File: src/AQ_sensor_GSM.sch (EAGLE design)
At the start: 260 parts, among them J1 F-1X03-SIP-100-32, J2 53261-0871, J4 S8411-45R, Q2 MMBT2222, Q3 MMBT2222, Q4 MMBT2222, Q5 MMBT2222, Q6 MMBT2222, Q7 MMBT2222, Q8 FS8205, T1 S8050, T2 S8050, U1 CP2102N-A02-GQFN28, U2 DS1307Z, U3 TP4056, U4 TPS63802DLAR, U5 TXS0108EPWR, U6 TPS63802DLAR, X1 ESP32-S3-WROOM-1-N16R8, Y1 32.768kHz

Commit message: Routing in Progress
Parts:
- removed R40: 10K, rcl:R-EU_R0603
- added C37, C38: 0.1uF, rcl:C-EUC0603
- added L4: 784778010, Fixed Inductors:784778010
- added POWER: 10118192-0001LF, AQ_sensor_GSM:10118192-0001LF
- added R62: 100k, SparkFun-Resistors:1.20KOHM-0603-1/10W-1%
- added R63: 432k, SparkFun-Resistors:1.20KOHM-0603-1/10W-1%
- added R64: 47k, SparkFun-Resistors:1.20KOHM-0603-1/10W-1%
- added R65: 1k, SparkFun-Resistors:1.20KOHM-0603-1/10W-1%
- added R66, R67: 10K, rcl:R-EU_R0603
- added U7: TPS63802DLAR, TPS63802DLAR:TPS63802DLAR
- C21: device SparkFun-Capacitors:220PF-0402T-50V-5% -> rcl:C-EUC0603
- C26: value 22pF -> TAJB106K016RNJ; device SparkFun-Capacitors:220PF-0402T-50V-5% -> Resistor_Capacitor:TAJB106K016RNJ
- C28: value TAJB106K016RNJ -> 22pF; device Resistor_Capacitor:TAJB106K016RNJ -> rcl:C-EUC0603
- C32: value 0.1uF -> TAJB106K016RNJ; device rcl:C-EUC0603 -> Resistor_Capacitor:TAJB106K016RNJ
- renumbered 5V_IN1 to FULL, 5V_IN2 to CHRG, USB to 3.3IND
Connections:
- removed net IO15: R40.1, X1.IO15
- removed net IO5: X1.IO5
- removed net IO6: X1.IO6
- removed net IO7: X1.IO7
- removed net IO8: X1.IO8
- removed net LBV: R10.2
- removed net L_MIS0: U$1.MISO, X1.IO2
- removed net L_MOSI: U$1.MOSI, X1.IO1
- removed net L_SCK: U$1.SCK, X1.IO3
- removed net SD_CLK: MICRO_SD1.CLK, X1.IO38
- removed net SD_MISO: MICRO_SD1.CMD, X1.IO41
- removed net SD_MOSI: MICRO_SD1.DAT0, X1.IO40
- new net IO21: X1.IO21
- new net IO35: X1.IO35
- new net IO36: X1.IO36
- new net IO37: X1.IO37
- new net IO38: X1.IO38
- new net IO40: X1.IO40
- new net IO41: X1.IO41
- new net IO42: X1.IO42
- new net IO45: R66.1, X1.IO45
- new net IO46: R67.1, X1.IO46
- new net MISO: MICRO_SD1.CMD, U$1.MISO, X1.IO2
- new net MOSI: MICRO_SD1.DAT0, U$1.MOSI, X1.IO1
- new net N$149: L4.2, U7.L1
- new net N$150: L4.1, U7.L2
- new net N$151: R62.1, U7.PG
- new net N$152: R63.2, R64.1, U7.FB
- new net SPI_CLK: MICRO_SD1.CLK, U$1.SCK, X1.IO3
- net 12V-IN: now also C26.1, C28.1, C37.1, R62.2, R65.2, U7.VIN; no longer C21.1
- net 4.0V_OUT: now also C10.1, C11.1, C12.1, C13.2, C14.2, C2.1, C5.2, C6.1, C9.1, D2.K, EC200_GSM.VBAT_BB, EC200_GSM.VBAT_RF, MODE.A, MRI.A, NST.A, PST.A, R502.2
- net BOOST_EN: now also R65.1, U7.EN
- net DHT_LED: no longer X1.IO37
- net DHT_OUT: now also X1.IO7; no longer X1.IO36
- net GND: now also C37.2, C38.2, POWER.GND, POWER.ID, POWER.SHIELD, R64.2, R66.2, R67.2, U7.AGND, U7.GND, U7.MODE; no longer R40.2
- net GSM_RST_O: now also X1.IO15; no longer X1.IO42
- net L_NSS: now also X1.IO8; no longer X1.IO46
- net N$138: no longer C28.1, C32.1
- net PMS_LED: no longer X1.IO35
- net PMS_RX: now also X1.IO5; no longer X1.IO21
- net PMS_TX: now also X1.IO6; no longer X1.IO45
- net VUSB: now also C21.1, C32.1, C38.1, POWER.VUSB, R63.1, U7.VOUT; no longer C26.1
- net V_LIPO: now also R10.2; no longer C10.1, C11.1, C12.1, C13.2, C14.2, C2.1, C5.2, C6.1, C9.1, D2.K, EC200_GSM.VBAT_BB, EC200_GSM.VBAT_RF, MODE.A, MRI.A, NST.A, PST.A, R502.2
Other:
- note added: "5V In Buck CIRCUIT"
- moved on the sheet: C21, C26, C27, C28, C32, GRST, GSM_RST, MODE, MRI, NST, PST, Q4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

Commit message: 90% routed
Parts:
- removed DHT: GREEN, led:LEDCHIP-LED0603
- removed PMS: ORANGE, led:LEDCHIP-LED0603
- removed R11, R49: 200, rcl:R-EU_R0603
- removed R16, R4: 470R, rcl:R-EU_R0603
- removed RXT, TXT: (no value), led:LEDCHIP-LED0603
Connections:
- removed net DHT_LED: R16.2
- removed net N$115: U$69.P$1, U1.GPIO.3/WAKEUP
- removed net N$116: U$68.P$1, U1.GPIO.4
- removed net N$117: U$67.P$1, U1.GPIO.5
- removed net N$118: U$66.P$1, U1.GPIO.6
- removed net PMS_LED: R4.2
- net +3V3: no longer R11.2, R49.2
- net GND: no longer DHT.C, PMS.C, RST2.SHIELD
- net N$114: now also U$71.P$1, U1.GPIO.6; no longer U$70.P$1, U1.GPIO.2/RS485
- net N$27: now also U$70.P$1, U1.GPIO.1/RXT; no longer DHT.A, R16.1
- net N$4: now also U$72.P$1, U1.GPIO.0/TXT; no longer PMS.A, R4.1
- net N$54: now also U$69.P$1, U1.GPIO.2/RS485; no longer R11.1, TXT.C
- net N$55: now also U$68.P$1, U1.GPIO.3/WAKEUP; no longer R49.1, RXT.C
- net N$56: now also U$67.P$1, U1.GPIO.4; no longer TXT.A, U1.GPIO.0/TXT
- net N$57: now also U$66.P$1, U1.GPIO.5; no longer RXT.A, U1.GPIO.1/RXT
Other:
- note removed: "IO6 TO IO11 ARE USED BY SPIFFS AND CANT BE USED"

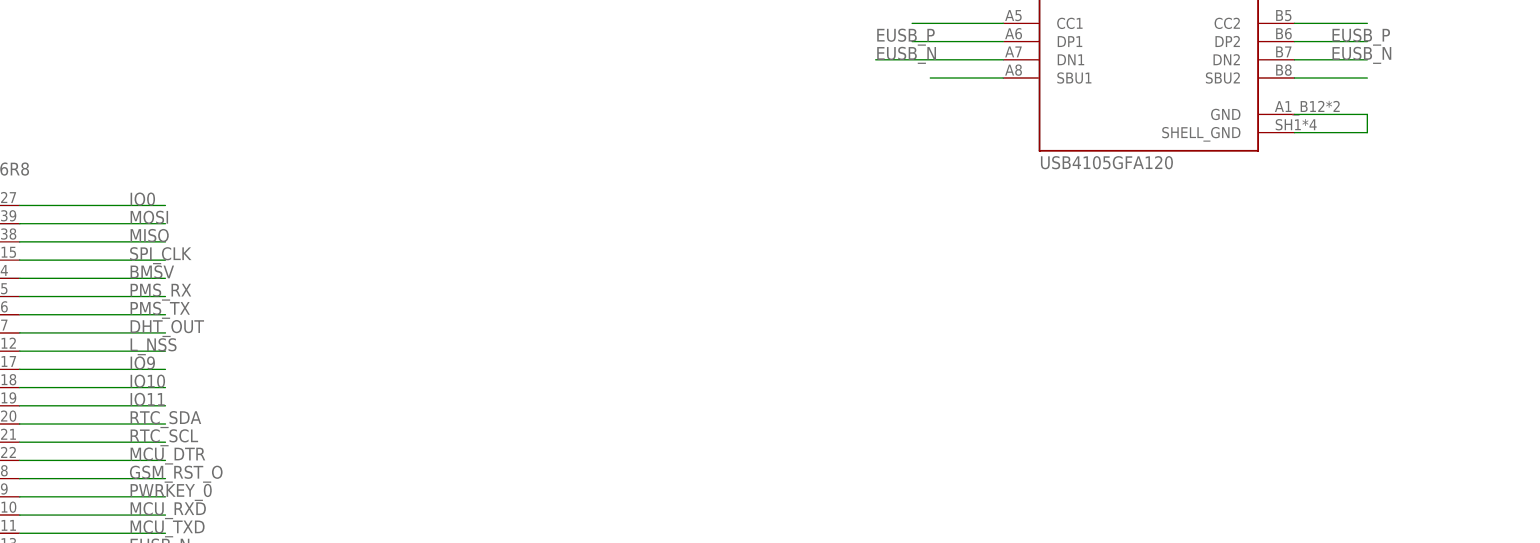
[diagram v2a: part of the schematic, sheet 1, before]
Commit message: 100% routed Minus Board Outline
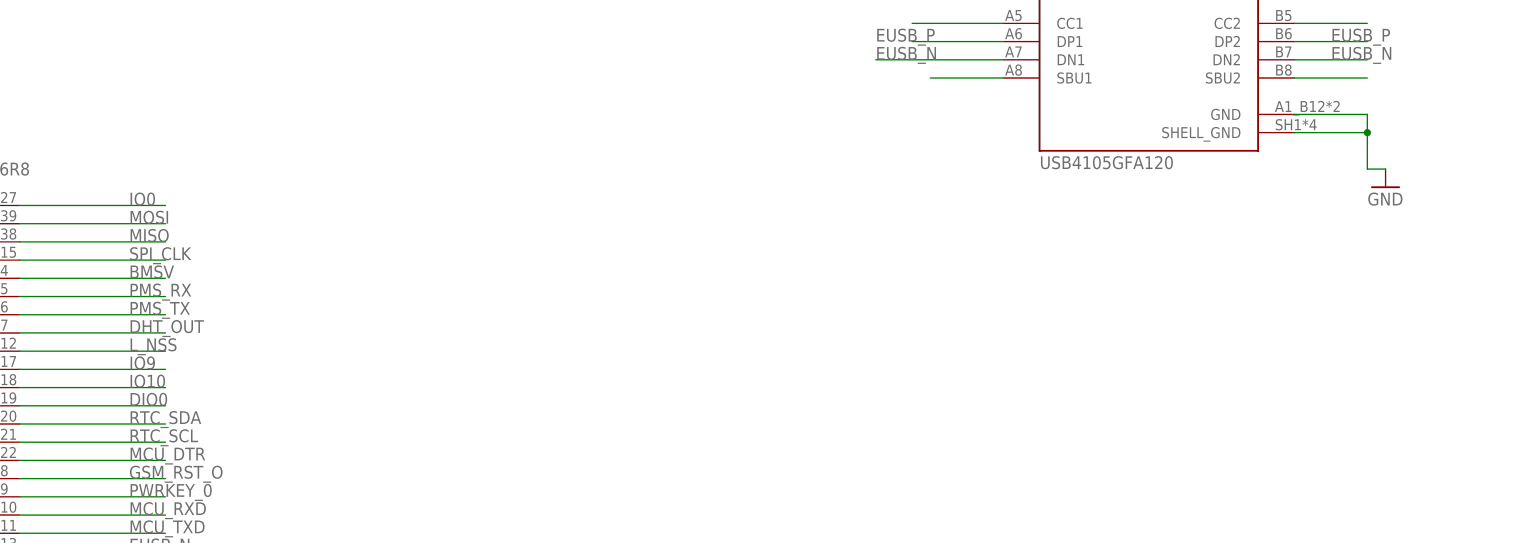
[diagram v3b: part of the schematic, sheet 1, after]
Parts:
- removed U$75: NC_MARKER, NC_MARKER:NC_MARKER
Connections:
- removed net IO11: X1.IO11
- removed net N$128: U$1.DIO0, U$75.P$1
- removed net N$140: JTAG.GND, JTAG.SHELL_GND
- new net DIO0: U$1.DIO0, X1.IO11
- net GND: now also JTAG.GND, JTAG.SHELL_GND
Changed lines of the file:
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@@
 <part name="U$73" library="NC_MARKER" deviceset="NC_MARKER" device=""/>
 <part name="U$74" library="NC_MARKER" deviceset="NC_MARKER" device=""/>
-<part name="U$75" library="NC_MARKER" deviceset="NC_MARKER" device=""/>
 <part name="U$76" library="NC_MARKER" deviceset="NC_MARKER" device=""/>
 <part name="U$77" library="NC_MARKER" deviceset="NC_MARKER" device=""/>
@@
 <part name="GND97" library="supply1" library_urn="urn:adsk.eagle:library:371" deviceset="GND" device=""/>
 <part name="R67" library="rcl" library_urn="urn:adsk.eagle:library:334" deviceset="R-EU_" device="R0603" package3d_urn="urn:adsk.eagle:package:23555/3" value="10K"/>
+<part name="GND8" library="supply1" library_urn="urn:adsk.eagle:library:371" deviceset="GND" device=""/>
 </parts>
 <sheets>
@@
 <attribute name="VALUE" x="37.338" y="227.33" size="1.778" layer="96" rot="R270"/>
 </instance>
+<instance part="GND8" gate="1" x="281.94" y="165.1" smashed="yes">
+<attribute name="VALUE" x="279.4" y="162.56" size="1.778" layer="96"/>
+</instance>
 </instances>
 <busses>
@@
 <pinref part="R67" gate="G$1" pin="2"/>
 </segment>
+<segment>
+<pinref part="JTAG" gate="G$1" pin="SHELL_GND"/>
+<wire x1="269.24" y1="172.72" x2="279.4" y2="172.72" width="0.1524" layer="91"/>
+<wire x1="279.4" y1="172.72" x2="279.4" y2="175.26" width="0.1524" layer="91"/>
+<pinref part="JTAG" gate="G$1" pin="GND"/>
+<wire x1="279.4" y1="175.26" x2="269.24" y2="175.26" width="0.1524" layer="91"/>
+<pinref part="GND8" gate="1" pin="GND"/>
+<wire x1="281.94" y1="167.64" x2="279.4" y2="167.64" width="0.1524" layer="91"/>
+<wire x1="279.4" y1="167.64" x2="279.4" y2="172.72" width="0.1524" layer="91"/>
+<junction x="279.4" y="172.72"/>
+</segment>
 </net>
 <net name="+3V3" class="1">
@@
 </segment>
 </net>
-<net name="IO11" class="0">
+<net name="DIO0" class="0">
 <segment>
 <pinref part="X1" gate="G$1" pin="IO11"/>
@@
 </segment>
 </net>
-<net name="N$140" class="0">
-<segment>
-<pinref part="JTAG" gate="G$1" pin="SHELL_GND"/>
-<wire x1="269.24" y1="172.72" x2="279.4" y2="172.72" width="0.1524" layer="91"/>
-<wire x1="279.4" y1="172.72" x2="279.4" y2="175.26" width="0.1524" layer="91"/>
-<pinref part="JTAG" gate="G$1" pin="GND"/>
-<wire x1="279.4" y1="175.26" x2="269.24" y2="175.26" width="0.1524" layer="91"/>
-</segment>
-</net>
 <net name="N$141" class="0">
 <segment>
@@
 <attribute name="VALUE" x="16.518" y="12.478" size="1.778" layer="96" rot="R270"/>
 </instance>
-<instance part="U$75" gate="G$1" x="27.94" y="10.16" smashed="yes"/>
 <instance part="U$76" gate="G$1" x="27.94" y="7.62" smashed="yes"/>
 <instance part="U$77" gate="G$1" x="27.94" y="5.08" smashed="yes"/>
@@
 </segment>
 </net>
-<net name="N$128" class="0">
+<net name="DIO0" class="0">
 <segment>
-<pinref part="U$75" gate="G$1" pin="P$1"/>
 <pinref part="U$1" gate="G$1" pin="DIO0"/>
 <wire x1="33.02" y1="10.16" x2="35.56" y2="10.16" width="0.1524" layer="91"/>
+<label x="27.94" y="10.16" size="1.778" layer="95"/>
 </segment>
 </net>

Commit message: Resolved multiple shared output pins
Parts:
- added R11, R4: 0.4R, Resistor_Capacitor:CRCW08050000Z0EA
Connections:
- new net N$115: R4.2, U7.VOUT
- new net N$116: 5V_REG_1.OUTPUT, R11.2
- net VUSB: now also R11.1, R4.1; no longer 5V_REG_1.OUTPUT, U7.VOUT
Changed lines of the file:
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@@
 <setting verticaltext="up"/>
 </settings>
-<grid distance="0.1" unitdist="inch" unit="inch" style="lines" multiple="1" display="no" altdistance="0.01" altunitdist="inch" altunit="inch"/>
+<grid distance="0.1" unitdist="inch" unit="inch" style="lines" multiple="1" display="no" altdistance="0.01" altunitdist="inch" altunit="mm"/>
 <layers>
 <layer number="1" name="Top" color="4" fill="1" visible="no" active="no"/>
@@
 <part name="R67" library="rcl" library_urn="urn:adsk.eagle:library:334" deviceset="R-EU_" device="R0603" package3d_urn="urn:adsk.eagle:package:23555/3" value="10K"/>
 <part name="GND8" library="supply1" library_urn="urn:adsk.eagle:library:371" deviceset="GND" device=""/>
+<part name="R4" library="Resistor_Capacitor" library_urn="urn:adsk.eagle:library:15122775" deviceset="CRCW08050000Z0EA" device="" package3d_urn="urn:adsk.eagle:package:10872899/3" value="0.4R"/>
+<part name="R11" library="Resistor_Capacitor" library_urn="urn:adsk.eagle:library:15122775" deviceset="CRCW08050000Z0EA" device="" package3d_urn="urn:adsk.eagle:package:10872899/3" value="0.4R"/>
 </parts>
 <sheets>
@@
 <attribute name="VALUE" x="48.26848125" y="393.7" size="1.78096875" layer="96" rot="R90"/>
 </instance>
-<instance part="GND13" gate="1" x="22.86" y="324.358" smashed="yes">
-<attribute name="VALUE" x="20.32" y="321.818" size="1.778" layer="96"/>
+<instance part="GND13" gate="1" x="35.56" y="324.358" smashed="yes">
+<attribute name="VALUE" x="33.02" y="321.818" size="1.778" layer="96"/>
 </instance>
 <instance part="U3" gate="G$1" x="-142.24" y="347.98" smashed="yes">
@@
 <attribute name="VALUE" x="104.14" y="260.604" size="1.778" layer="96" font="vector" rot="R180" align="top-center"/>
 </instance>
+<instance part="R4" gate="G$1" x="149.86" y="264.16" smashed="yes" rot="R180">
+<attribute name="NAME" x="153.67" y="262.6614" size="1.778" layer="95" rot="R180"/>
+<attribute name="VALUE" x="153.67" y="267.462" size="1.778" layer="96" rot="R180"/>
+</instance>
+<instance part="R11" gate="G$1" x="-236.22" y="373.38" smashed="yes" rot="R180">
+<attribute name="NAME" x="-232.41" y="371.8814" size="1.778" layer="95" rot="R180"/>
+<attribute name="VALUE" x="-232.41" y="376.682" size="1.778" layer="96" rot="R180"/>
+</instance>
 </instances>
 <busses>
@@
 </segment>
 <segment>
-<pinref part="GND13" gate="1" pin="GND"/>
-<wire x1="22.86" y1="326.898" x2="22.86" y2="329.946" width="0.1524" layer="91"/>
-<pinref part="C12" gate="G$1" pin="2"/>
-<pinref part="C9" gate="G$1" pin="2"/>
-<wire x1="24.384" y1="329.946" x2="35.56" y2="329.946" width="0.1524" layer="91"/>
-<junction x="24.384" y="329.946"/>
-<wire x1="12.7" y1="329.946" x2="24.384" y2="329.946" width="0.1524" layer="91"/>
-<pinref part="C13" gate="G$1" pin="1"/>
-<wire x1="12.7" y1="330.2" x2="12.7" y2="329.946" width="0.1524" layer="91"/>
-<junction x="12.7" y="330.2"/>
-<wire x1="2.54" y1="330.2" x2="12.7" y2="330.2" width="0.1524" layer="91"/>
-<pinref part="C2" gate="G$1" pin="2"/>
-<wire x1="22.86" y1="330.2" x2="22.86" y2="329.946" width="0.1524" layer="91"/>
-<wire x1="22.86" y1="329.946" x2="24.384" y2="329.946" width="0.1524" layer="91"/>
-</segment>
-<segment>
 <pinref part="GND1" gate="1" pin="GND"/>
 <wire x1="-238.76" y1="362.458" x2="-238.76" y2="365.76" width="0.1524" layer="91"/>
@@
 <wire x1="162.56" y1="236.22" x2="162.56" y2="238.76" width="0.1524" layer="91"/>
 </segment>
+<segment>
+<pinref part="C2" gate="G$1" pin="2"/>
+<pinref part="C13" gate="G$1" pin="1"/>
+<wire x1="2.54" y1="330.2" x2="12.7" y2="330.2" width="0.1524" layer="91"/>
+<pinref part="C9" gate="G$1" pin="2"/>
+<wire x1="12.7" y1="330.2" x2="12.7" y2="329.946" width="0.1524" layer="91"/>
+<wire x1="12.7" y1="329.946" x2="24.384" y2="329.946" width="0.1524" layer="91"/>
+<junction x="12.7" y="330.2"/>
+<pinref part="C12" gate="G$1" pin="2"/>
+<wire x1="24.384" y1="329.946" x2="35.56" y2="329.946" width="0.1524" layer="91"/>
+<junction x="24.384" y="329.946"/>
+<pinref part="GND13" gate="1" pin="GND"/>
+<wire x1="35.56" y1="326.898" x2="35.56" y2="329.946" width="0.1524" layer="91"/>
+<junction x="35.56" y="329.946"/>
+</segment>
 </net>
 <net name="V_LIPO" class="3">
@@
 </segment>
 <segment>
-<pinref part="5V_REG_1" gate="G$1" pin="OUTPUT"/>
-<wire x1="-246.38" y1="373.38" x2="-238.76" y2="373.38" width="0.1524" layer="91"/>
-<label x="-243.84" y="373.38" size="1.778" layer="95"/>
-</segment>
-<segment>
 <pinref part="5V_JST" gate="G$1" pin="1"/>
 <wire x1="-276.86" y1="304.8" x2="-292.1" y2="304.8" width="0.1524" layer="91"/>
@@
 </segment>
 <segment>
-<pinref part="U7" gate="G$1" pin="VOUT"/>
 <pinref part="C38" gate="G$1" pin="1"/>
-<wire x1="142.24" y1="264.16" x2="162.56" y2="264.16" width="0.1524" layer="91"/>
 <wire x1="162.56" y1="264.16" x2="172.72" y2="264.16" width="0.1524" layer="91"/>
 <wire x1="172.72" y1="264.16" x2="172.72" y2="259.08" width="0.1524" layer="91"/>
@@
 <pinref part="R63" gate="G$1" pin="1"/>
 <wire x1="162.56" y1="261.62" x2="162.56" y2="264.16" width="0.1524" layer="91"/>
-<junction x="162.56" y="264.16"/>
 <wire x1="180.34" y1="264.16" x2="198.12" y2="264.16" width="0.1524" layer="91"/>
 <junction x="180.34" y="264.16"/>
 <label x="187.96" y="264.16" size="1.778" layer="95"/>
+<pinref part="R4" gate="G$1" pin="1"/>
+<wire x1="154.94" y1="264.16" x2="162.56" y2="264.16" width="0.1524" layer="91"/>
+<junction x="162.56" y="264.16"/>
+</segment>
+<segment>
+<pinref part="R11" gate="G$1" pin="1"/>
+<wire x1="-231.14" y1="373.38" x2="-223.52" y2="373.38" width="0.1524" layer="91"/>
+<label x="-228.6" y="373.38" size="1.778" layer="95"/>
 </segment>
 </net>
@@
 <pinref part="C13" gate="G$1" pin="2"/>
 <wire x1="2.54" y1="337.82" x2="12.7" y2="337.82" width="0.1524" layer="91"/>
-<wire x1="12.7" y1="337.82" x2="12.7" y2="345.44" width="0.1524" layer="91"/>
+<wire x1="12.7" y1="337.82" x2="12.7" y2="340.36" width="0.1524" layer="91"/>
+<wire x1="12.7" y1="340.36" x2="12.7" y2="345.44" width="0.1524" layer="91"/>
 <wire x1="12.7" y1="345.44" x2="25.4" y2="345.44" width="0.1524" layer="91"/>
 <junction x="12.7" y="337.82"/>
@@
 <pinref part="C2" gate="G$1" pin="1"/>
 <pinref part="C12" gate="G$1" pin="1"/>
-<wire x1="35.56" y1="340.36" x2="35.56" y2="337.566" width="0.1524" layer="91"/>
+<wire x1="35.56" y1="337.566" x2="35.56" y2="340.36" width="0.1524" layer="91"/>
+<wire x1="35.56" y1="340.36" x2="12.7" y2="340.36" width="0.1524" layer="91"/>
+<junction x="12.7" y="340.36"/>
 <pinref part="C9" gate="G$1" pin="1"/>
-<wire x1="35.56" y1="340.36" x2="24.384" y2="340.36" width="0.1524" layer="91"/>
-<wire x1="24.384" y1="340.36" x2="24.384" y2="337.566" width="0.1524" layer="91"/>
-<wire x1="24.384" y1="340.36" x2="12.7" y2="340.36" width="0.1524" layer="91"/>
-<wire x1="12.7" y1="340.36" x2="12.7" y2="337.82" width="0.1524" layer="91"/>
+<wire x1="24.384" y1="337.566" x2="35.56" y2="337.566" width="0.1524" layer="91"/>
+<junction x="35.56" y="337.566"/>
 </segment>
 </net>
@@
 </segment>
 </net>
+<net name="N$115" class="0">
+<segment>
+<pinref part="U7" gate="G$1" pin="VOUT"/>
+<pinref part="R4" gate="G$1" pin="2"/>
+<wire x1="144.78" y1="264.16" x2="142.24" y2="264.16" width="0.1524" layer="91"/>
+</segment>
+</net>
+<net name="N$116" class="0">
+<segment>
+<pinref part="5V_REG_1" gate="G$1" pin="OUTPUT"/>
+<pinref part="R11" gate="G$1" pin="2"/>
+<wire x1="-241.3" y1="373.38" x2="-246.38" y2="373.38" width="0.1524" layer="91"/>
+</segment>
+</net>

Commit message: Route PCB 100%
Add 5V buck boost converter for charging Side

Add boost converter for 4.0V voltage rail

Add 5V Boost converter for the 5V rail

Add 3.3V LDO to power MCU
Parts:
- added JUMP4V, JUMP5V, JUMPVL, R16, R40: 0.4R, Resistor_Capacitor:CRCW08050000Z0EA
- added U$100, U$101, U$102, U$103, U$104, U$105, U$106, U$75, U$85, U$86, U$87, U$88, U$89, U$90, U$91, U$92, U$93, U$94, U$95, U$96, U$97, U$98, U$99: NC_MARKER, NC_MARKER:NC_MARKER
- added U8: AMS1117-3.3, AMS1117-3.3:AMS1117-3.3
- LORA: value (none) -> NA
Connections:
- removed net G_GPIO1: EC200_GSM.GPIO1
- new net N$117: JUMPVL.1, R40.1, U8.VIN
- new net N$118: R16.2, U8.VOUT
- new net N$128: EC200_GSM.GPIO1, U$75.P$1
- new net N$140: J2.1, U$103.P$1
- new net N$153: J2.2, U$102.P$1
- new net N$154: J2.3, U$104.P$1
- new net N$155: J2.6, U$105.P$1
- net +3V3: now also R16.1
- net 4.0V_OUT: now also JUMP4V.1
- net 5V_OUT: now also JUMP5V.1, R40.2
- net GND: now also U8.GND/ADJ
- net IO10: now also U$86.P$1
- net IO21: now also U$87.P$1
- net IO35: now also U$88.P$1
- net IO36: now also U$89.P$1
- net IO37: now also U$90.P$1
- net IO38: now also U$91.P$1
- net IO40: now also U$92.P$1
- net IO41: now also U$93.P$1
- net IO42: now also U$94.P$1
- net IO9: now also U$95.P$1
- net MCU_CTS: now also U$97.P$1
- net MCU_DCD: now also U$96.P$1
- net MCU_RI: now also U$85.P$1
- net MCU_RTS: now also U$98.P$1
- net N$12: now also U$99.P$1
- net N$139: now also U$100.P$1
- net N$141: now also U$101.P$1
- net N$144: now also U$106.P$1
- net V_LIPO: now also JUMP4V.2, JUMP5V.2, JUMPVL.2
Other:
- note added: "DO NOT SOLDER JUMP RESISTORS!"
